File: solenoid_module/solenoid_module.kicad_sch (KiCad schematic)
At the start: 6 parts, among them J1 1x5 2.54, J2 1x5 2.54, J3 1x2 5.08, J4 1x2 5.08, J5 1x3 5.08, SW1 3way switch

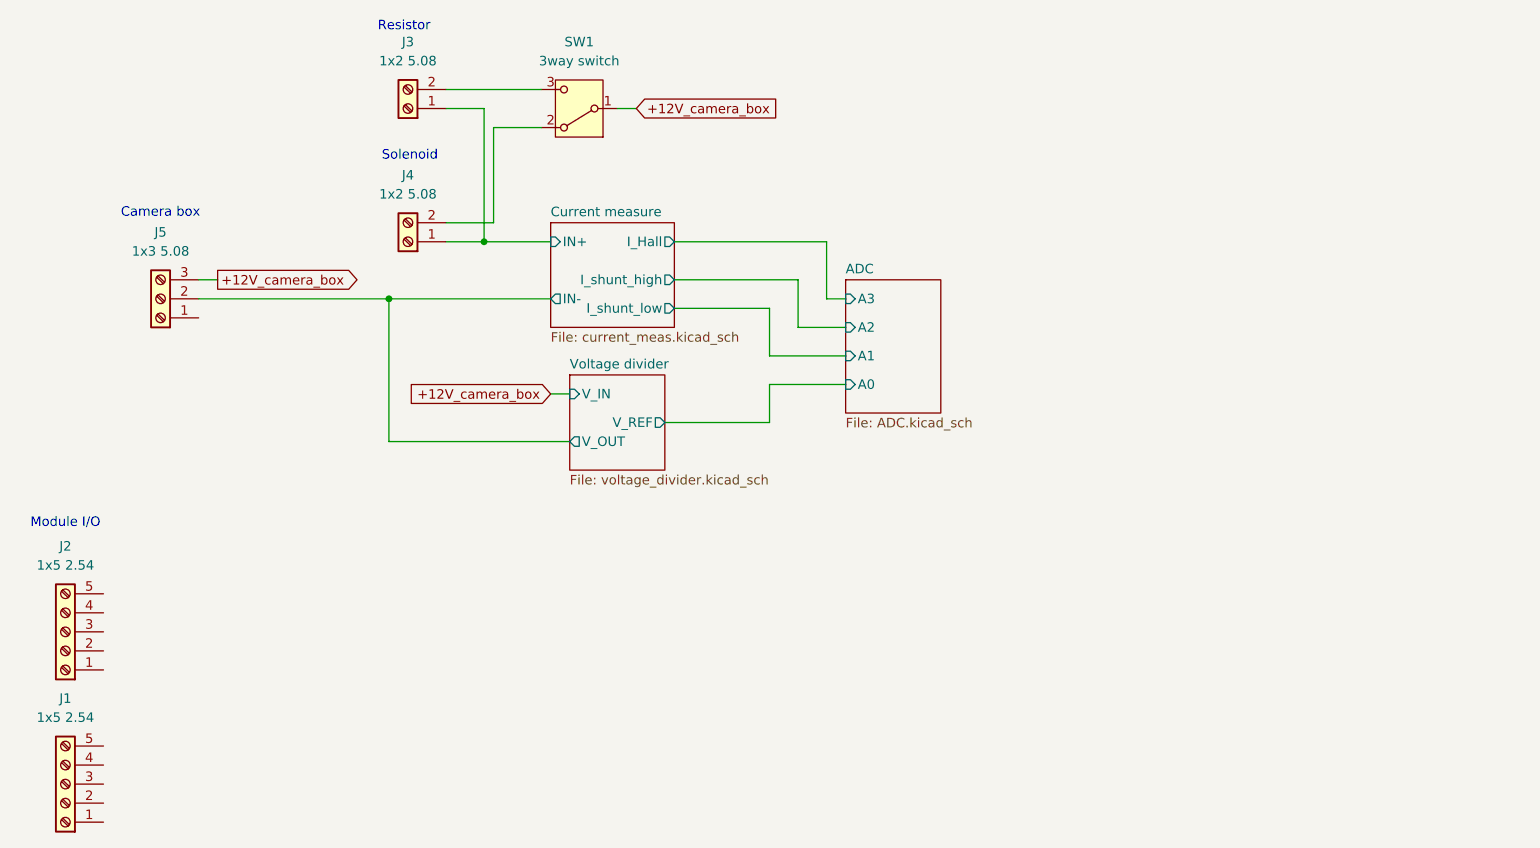
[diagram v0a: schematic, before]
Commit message: Solenoid module wiring
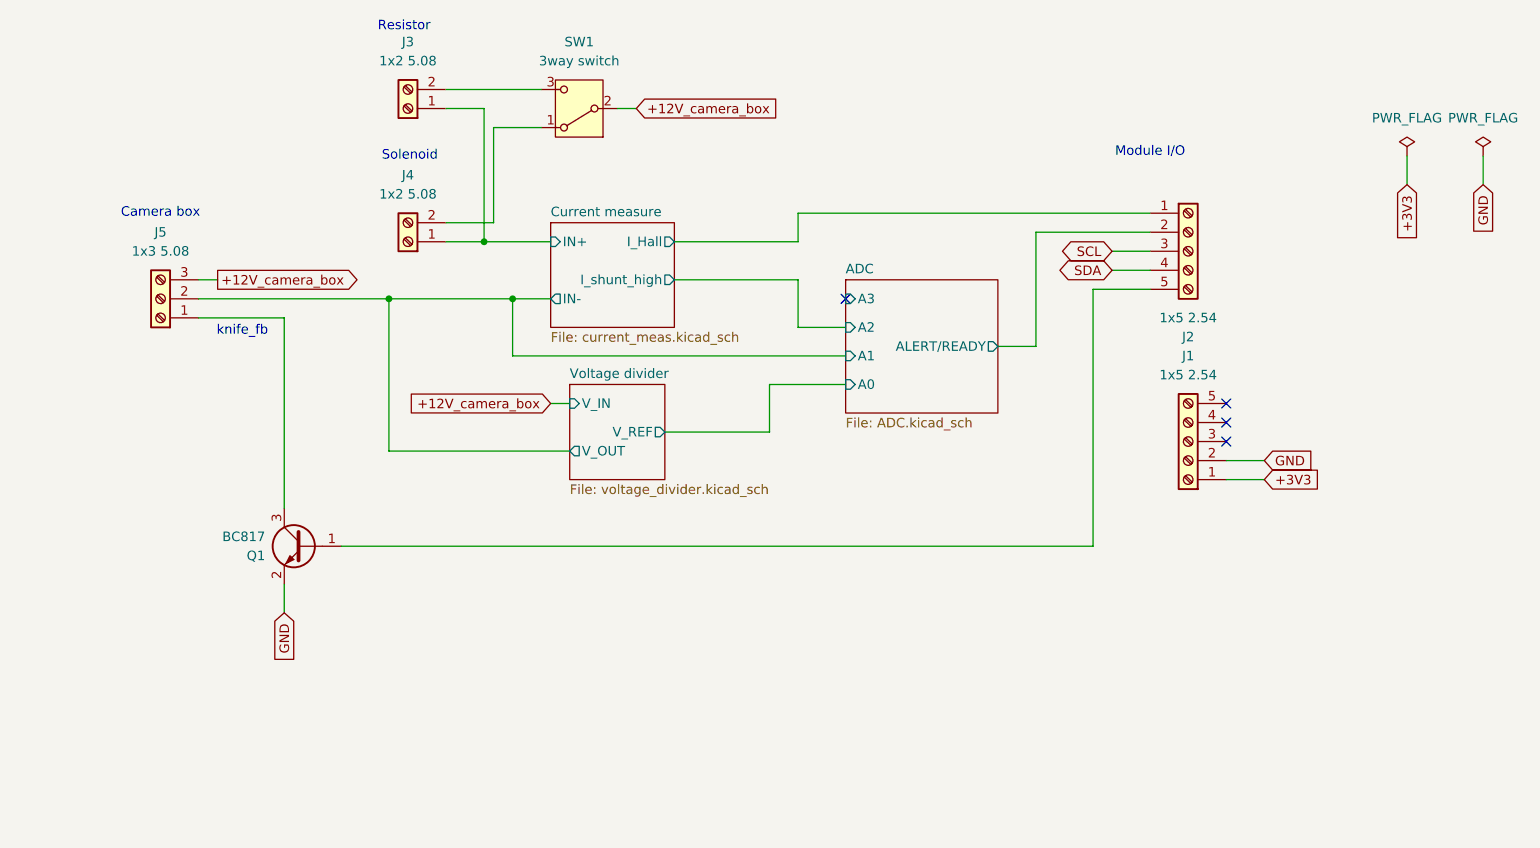
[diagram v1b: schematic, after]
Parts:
- added Q1: BC817, Package_TO_SOT_SMD:SOT-23, symbol Transistor_BJT:BC817
- J1, J2: footprint (none) -> Connector_PinHeader_2.54mm:PinHeader_1x05_P2.54mm_Vertical; Manufacturer Part Number (none) -> 68000-420HLF; Mouser Part Number (none) -> 649-68000-420HLF
- J3, J4: footprint (none) -> TerminalBlock_MetzConnect:TerminalBlock_MetzConnect_Type101_RT01602HBWC_1x02_P5.08mm_Horizontal; Manufacturer Part Number (none) -> TB0012-508-02GR; Mouser Part Number (none) -> 179-TB0012-508-02GR
- J5: footprint (none) -> TerminalBlock_MetzConnect:TerminalBlock_MetzConnect_Type101_RT01603HBWC_1x03_P5.08mm_Horizontal; Manufacturer Part Number (none) -> TB0012-508-03GR; Mouser Part Number (none) -> 179-TB0012-508-03GR
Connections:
- net Current measure/IN- is gone; now on net ADC/A1: J5.2 (Pin_2)
- net +12V_camera_box: now also SW1.2 (B); no longer SW1.1 (B)
- net at J4.2 (Pin_2): now also SW1.1 (A); no longer SW1.2 (A)
- net Current measure/I_Hall: now reaches J2.1 (Pin_1)
- net ADC/ALERT/READY: now reaches J2.2 (Pin_2)
- net SCL: now reaches J2.3 (Pin_3)
- net SDA: now reaches J2.4 (Pin_4)
- net at J2.5 (Pin_5): now also Q1.1 (B)
- net at J5.1 (Pin_1): now also Q1.3 (C)
- net +3V3: now reaches J1.1 (Pin_1)
- net GND: now reaches J1.2 (Pin_2)
- net GND: now also Q1.2 (E)
- no-connect marks 0 -> 4
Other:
- sheet ADC ports: added ALERT/READY; removed none
- sheet Current measure ports: added none; removed I_shunt_low
- note added: "knife_fb"
- moved on the sheet: J1, J2

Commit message: solenoid module pcb layout
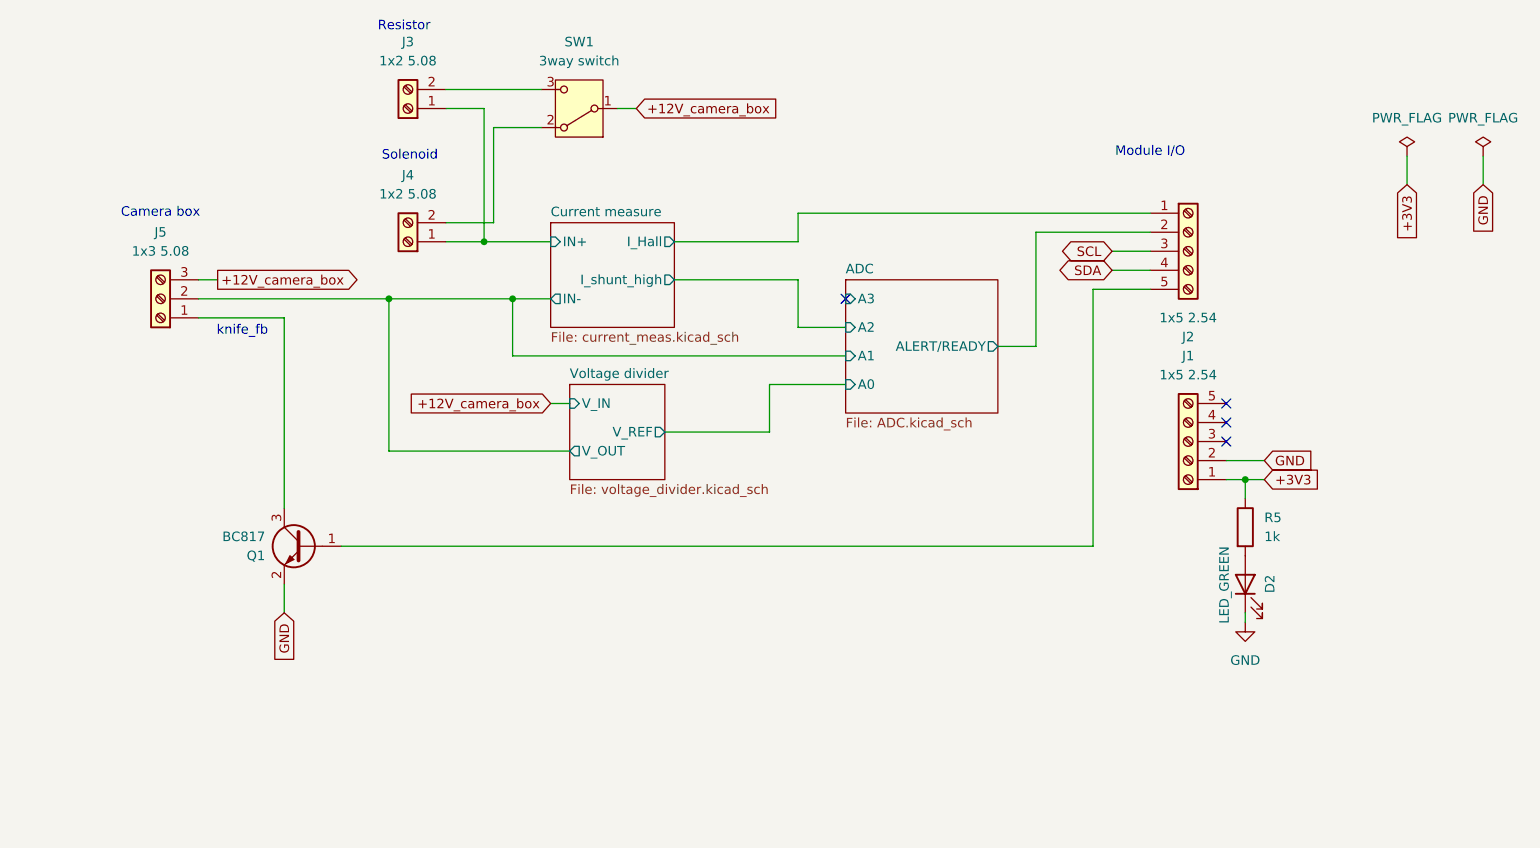
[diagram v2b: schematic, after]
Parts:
- added D2: LED_GREEN, LED_SMD:LED_0805_2012Metric_Pad1.15x1.40mm_HandSolder, symbol Device:LED
- added R5: 1k, Resistor_SMD:R_0603_1608Metric_Pad0.98x0.95mm_HandSolder, symbol Device:R
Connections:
- net +12V_camera_box: now also SW1.1 (B); no longer SW1.2 (B)
- net +3V3: now also R5.1
- net GND: now also D2.1 (K)
- net at J4.2 (Pin_2): now also SW1.2 (A); no longer SW1.1 (A)
- new net: D2.2 (A), R5.2

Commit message: PCB update
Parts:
- D2: Mouser Part Number (none) -> 604-APTD2012LCGCK
- R5: Mouser Part Number (none) -> 603-RC0603FR-071KL
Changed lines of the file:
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@@
+			)
+		)
+		(property "Mouser Part Number" "604-APTD2012LCGCK "
+			(at 220.98 140.97 0)
+			(effects
+				(font
+					(size 1.27 1.27)
+				)
+				(hide yes)
 			)
 		)
@@
 			(at 220.98 133.35 0)
 			(effects
+				(font
+					(size 1.27 1.27)
+				)
+				(hide yes)
+			)
+		)
+		(property "Mouser Part Number" "603-RC0603FR-071KL "
+			(at 220.98 133.35 0)
+			(effects
